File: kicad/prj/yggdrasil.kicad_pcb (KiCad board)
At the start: 2 copper layers, 186.8 x 135 mm, 44 parts, among them J2 4PIN, SW1 SW_PUSH, SW10 SW_PUSH, SW11 SW_PUSH, SW12 SW_PUSH, SW13 SW_PUSH, SW14 SW_PUSH, SW15 SW_PUSH, SW16 SW_PUSH, SW17 SW_PUSH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

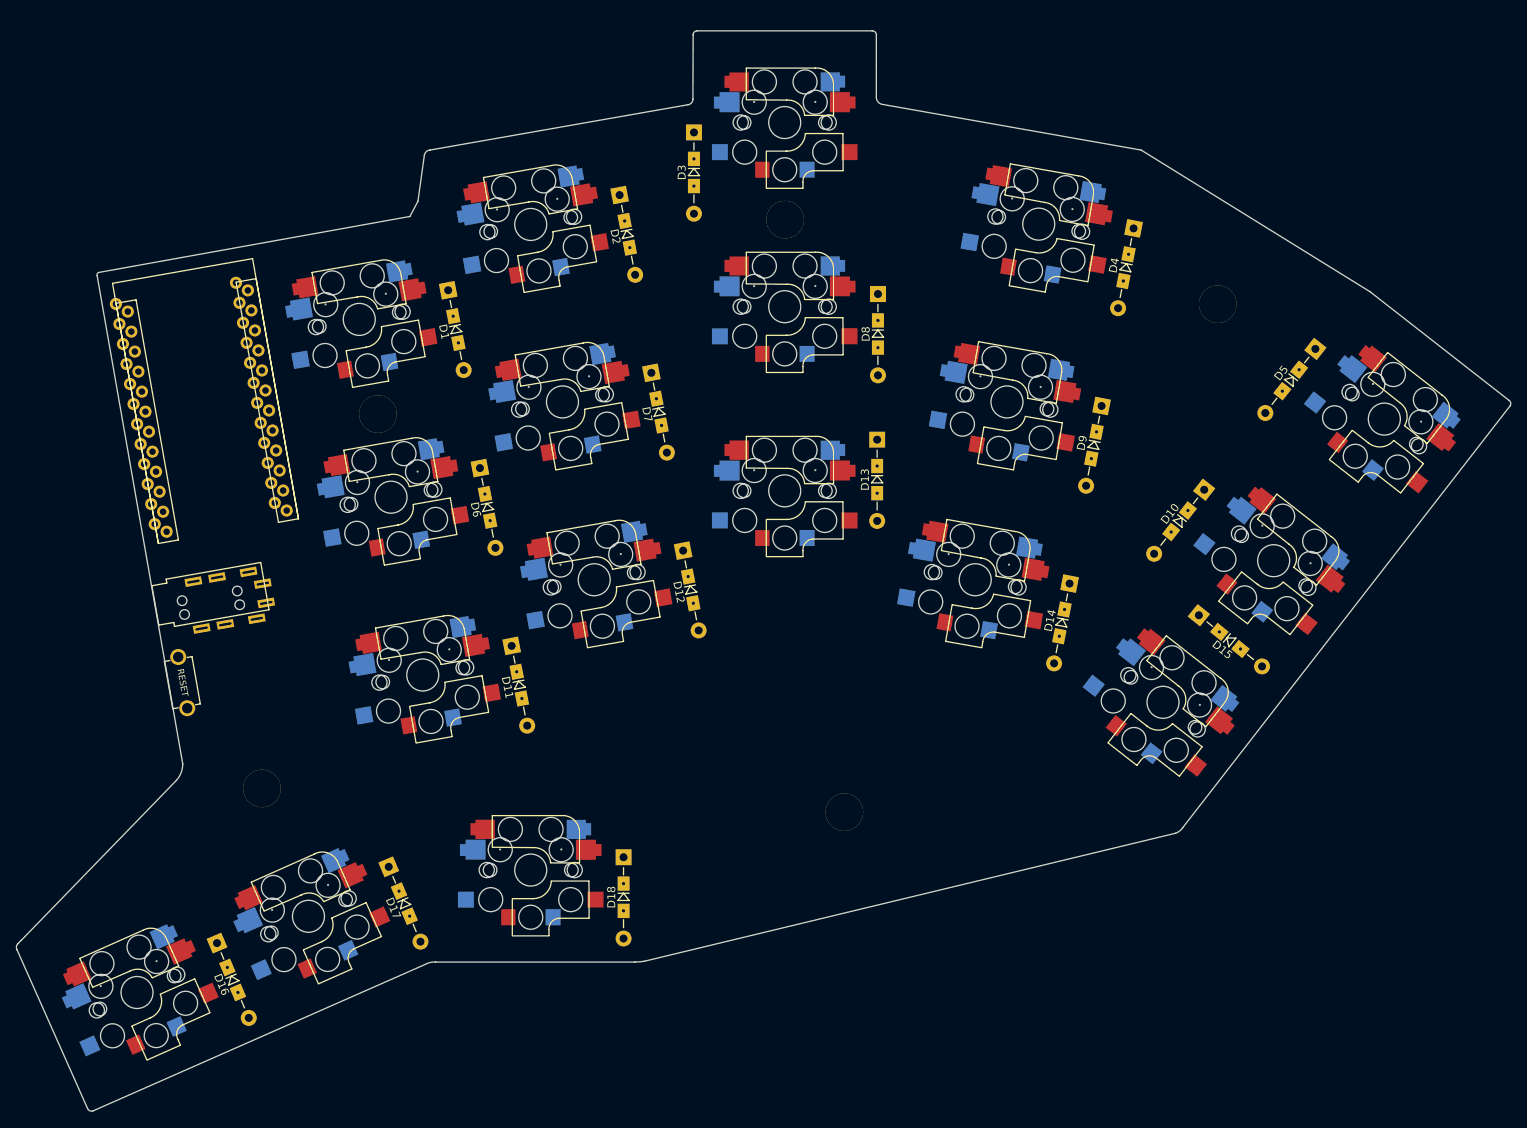
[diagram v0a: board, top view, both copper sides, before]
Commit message: Updated spacing Re-do edge cuts Some routing Diode placement Screwhole placement
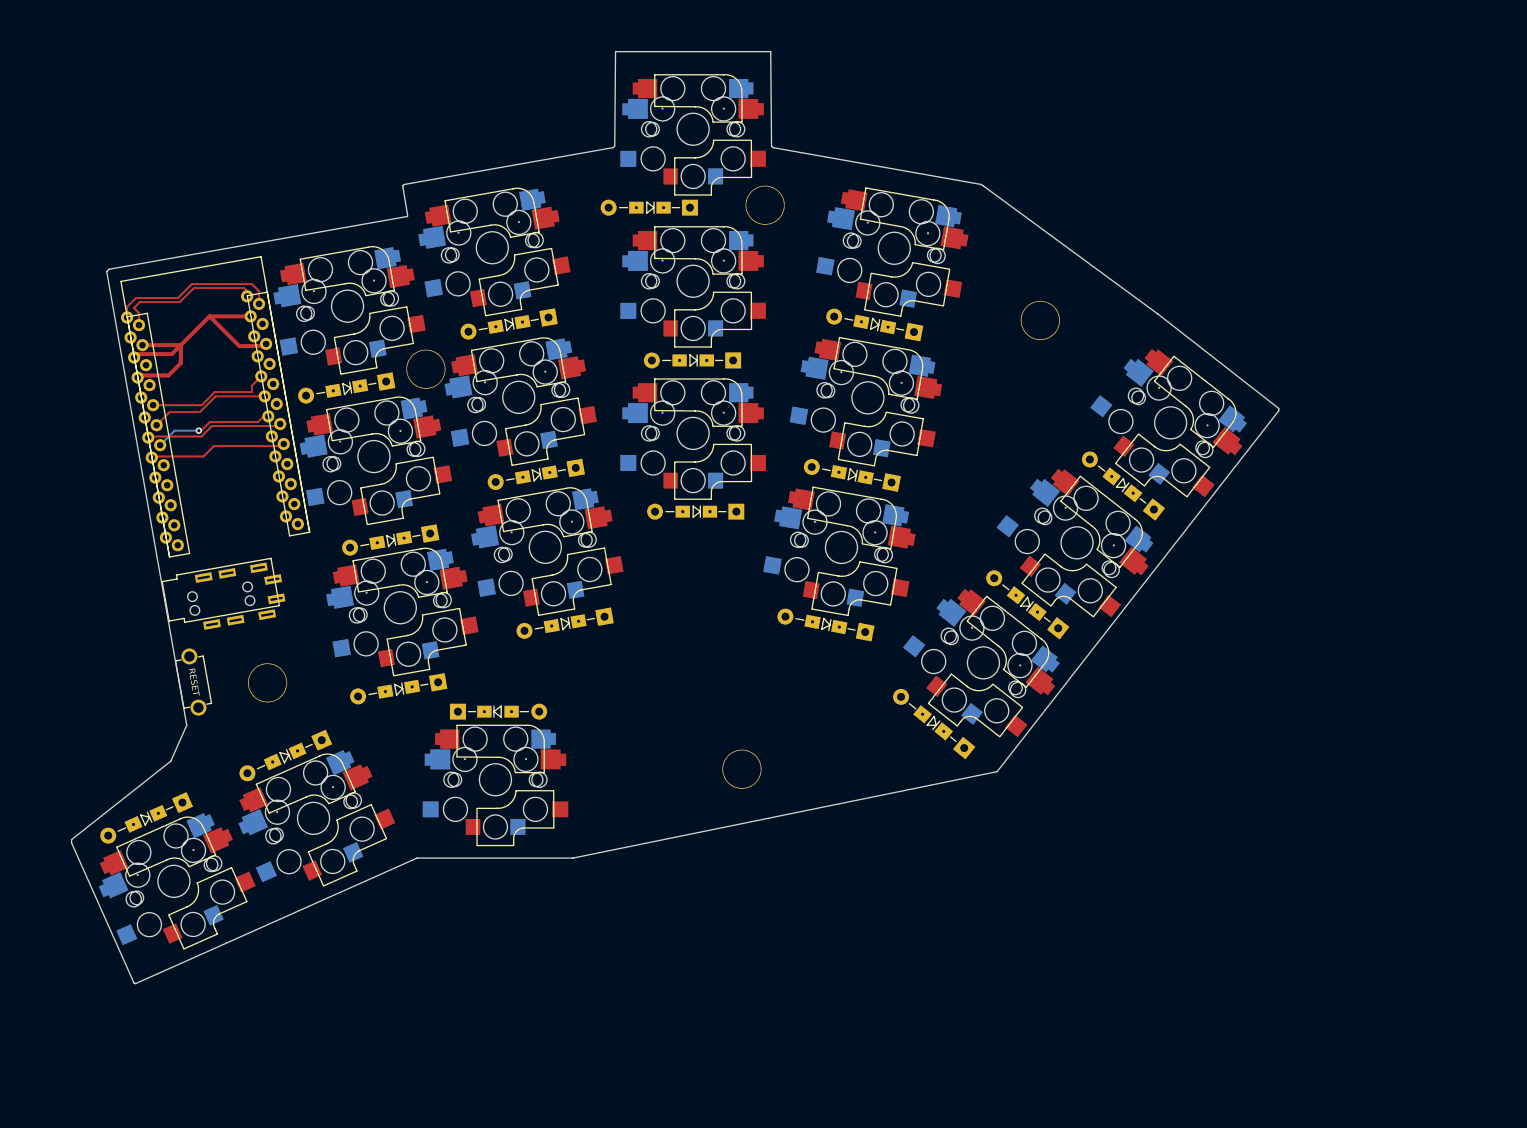
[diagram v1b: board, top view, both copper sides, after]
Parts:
- SW1, SW10, SW11, SW12, SW13, SW14, SW15, SW16, SW17, SW18, SW2, SW3, SW4, SW5, SW6, SW7, SW8, SW9: footprint Lily58-footprint:MX_Choc_Hotswap -> yggdrasil:Cherry_MX_Choc_Hotswap_MX_Spacing
- U1: footprint Lily58-footprint:ProMicro_rev2 -> yggdrasil:ProMicro_USB_C
- moved SW5 42.2 mm to (209.6, 85.0)
- moved SW10 40.0 mm to (197.9, 100.0)
- moved D15 38.5 mm to (195.4, 120.6), turned to 141 degrees
- moved SW15 38.0 mm to (186.2, 115.0)
- moved SW4 33.0 mm to (177.8, 70.2)
- moved D4 32.2 mm to (188.1, 70.8), turned to 169 degrees
- moved SW9 31.3 mm to (174.5, 88.9)
- moved D9 30.4 mm to (185.3, 89.6), turned to 169 degrees
- moved SW14 29.9 mm to (171.2, 107.6)
- moved D14 29.5 mm to (182.0, 108.3), turned to 169 degrees
- moved D18 28.0 mm to (141.0, 119.2), turned to 0 degrees
- moved SW3 25.4 mm to (154.4, 57.4)
- moved D5 24.8 mm to (219.1, 90.9), turned to 142 degrees
- moved SW8 23.8 mm to (154.4, 76.4)
- moved D17 23.7 mm to (114.4, 124.8), turned to -156 degrees
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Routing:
- net GND: track 0.00 -> 38.6 mm
- net unconnected-(U1-Pad1): track 0.00 -> 21.0 mm
- net unconnected-(U1-Pad24): track 0.00 -> 18.4 mm
- net unconnected-(U1-Pad8): track 0.00 -> 17.2 mm
- net unconnected-(U1-Pad7): track 0.00 -> 17.2 mm
- net unconnected-(U1-Pad20): track 0.00 -> 15.5 mm
- net unconnected-(U1-Pad19): track 0.00 -> 15.0 mm
- net unconnected-(U1-Pad18): track 0.00 -> 15.0 mm, vias 0 -> 1
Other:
- board size 186.8 x 135 mm -> 150.9 x 116.5 mm

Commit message: Change switch keycap spacing Add routing Add ground plane Add logo & text
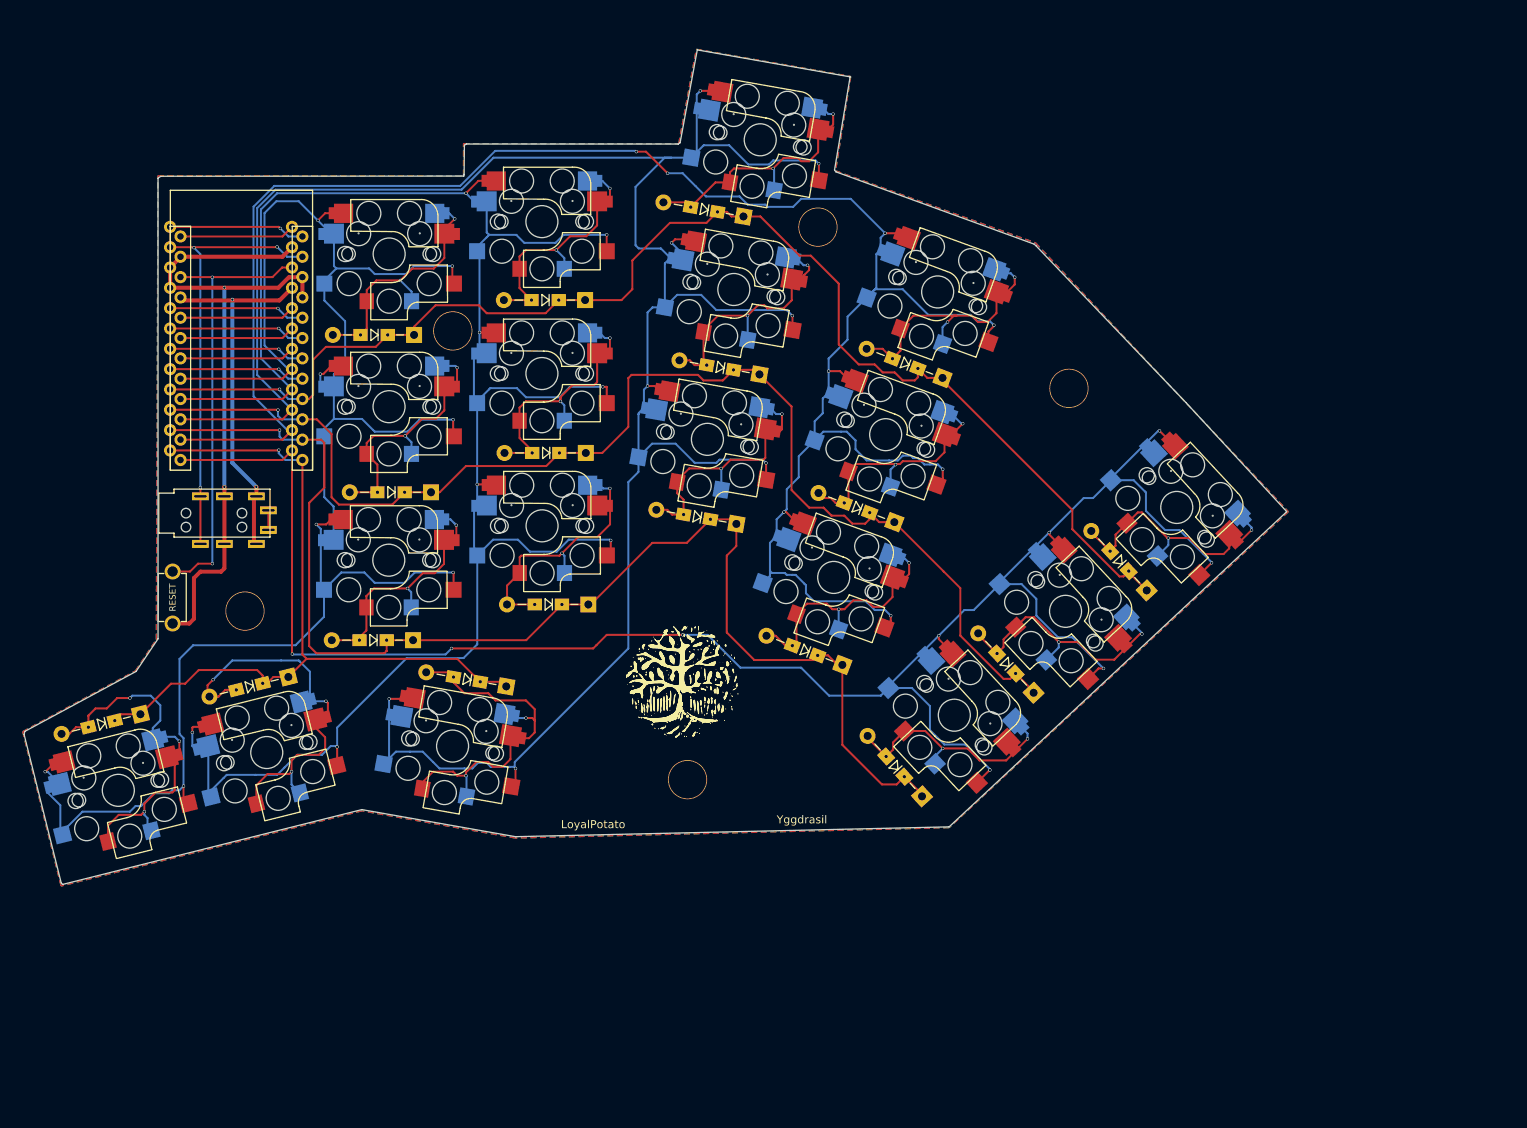
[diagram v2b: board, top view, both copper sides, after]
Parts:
- added G*** (x2): LOGO, yggdrasil:simple_logo, F.Cu at (164.1, 115.5)
- added G***: LOGO, yggdrasil:simple_logo, B.Cu at (164.1, 115.5)
- moved SW16 15.7 mm to (85.5, 142.4), turned to 14 degrees
- moved D16 13.1 mm to (91.5, 120.7), turned to -166 degrees
- moved SW17 12.5 mm to (104.1, 137.6), turned to 14 degrees
- moved U1 11.1 mm to (98.6, 89.0), turned to 0 degrees
- moved RSW1 10.9 mm to (100.3, 104.9), turned to 90 degrees
- moved J2 10.7 mm to (100.5, 94.4), turned to 90 degrees
- moved D17 9.80 mm to (109.9, 116.1), turned to -166 degrees
- moved D5 9.54 mm to (218.7, 100.4), turned to 133 degrees
- moved SW18 9.48 mm to (122.6, 132.4), turned to -10 degrees
- moved TH5 9.40 mm to (109.4, 106.6), turned to -10 degrees
- moved TH3 9.21 mm to (212.4, 78.8), turned to -10 degrees
- moved SW1 8.83 mm to (116.4, 73.0), turned to 0 degrees
- moved SW11 8.46 mm to (116.4, 111.3), turned to 0 degrees
- moved SW5 8.16 mm to (210.3, 93.1), turned to -47 degrees
- moved SW6 7.98 mm to (116.4, 92.1), turned to 0 degrees
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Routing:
- net col2: track 0.00 -> 309.3 mm, vias 0 -> 8
- net col3: track 0.00 -> 259.5 mm, vias 0 -> 8
- net col1: track 0.00 -> 255.4 mm, vias 0 -> 8
- net col0: track 0.00 -> 243.7 mm, vias 0 -> 8
- net col4: track 0.00 -> 241.3 mm, vias 0 -> 9
- net row0: track 0.00 -> 166.6 mm, vias 0 -> 1
- net row2: track 0.00 -> 162.6 mm, vias 0 -> 1
- net row1: track 0.00 -> 157.6 mm, vias 0 -> 1
- net row3: track 0.00 -> 97.9 mm, vias 0 -> 1
- net RESET: track 0.00 -> 55.6 mm, vias 0 -> 2
- net DATA: track 0.00 -> 54.4 mm, vias 0 -> 3
- net Net-(D17-Pad2): track 0.00 -> 52.1 mm, vias 0 -> 3
- net Net-(D16-Pad2): track 0.00 -> 47.5 mm, vias 0 -> 3
- net GND: track 38.6 -> 85.9 mm, vias 0 -> 2
- net VCC: track 0.00 -> 46.8 mm, vias 0 -> 2
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- added copper zone on B.Cu, net GND
- added copper zone on F.Cu, net GND
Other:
- board size 150.9 x 116.5 mm -> 157.8 x 104.3 mm
- board text added: "LoyalPotato"
- board text added: "Yggdrasil"

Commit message: Clean up/straighten routings
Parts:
- moved SW10 4.32 mm to (197.6, 102.0)
- moved D5 4.32 mm to (219.9, 96.2)
- moved J2 4.32 mm to (101.7, 90.2)
- moved D16 4.32 mm to (92.6, 116.6)
- moved SW18 4.32 mm to (123.8, 128.3)
- moved SW14 4.32 mm to (170.1, 104.8)
- moved D9 4.32 mm to (187.1, 89.6)
- moved D18 4.32 mm to (138.3, 111.0)
- moved D3 4.32 mm to (167.9, 52.3)
- moved G*** 4.32 mm to (165.3, 111.3) (x3)
- moved D4 4.32 mm to (193.1, 71.5)
- moved D12 4.32 mm to (148.5, 101.6)
- moved D10 4.32 mm to (205.7, 109.0)
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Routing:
- net col2: track 309.3 -> 297.2 mm
- net col3: track 259.5 -> 248.7 mm
- net col1: track 255.4 -> 261.9 mm
- net row0: track 166.6 -> 171.7 mm
- net Net-(D18-Pad2): track 46.0 -> 43.2 mm
- net Net-(D16-Pad2): track 47.5 -> 45.0 mm
- net Net-(D8-Pad2): track 34.0 -> 31.7 mm
- net col4: track 241.3 -> 239.6 mm
- net row3: track 97.9 -> 99.5 mm
- net Net-(D3-Pad2): track 36.1 -> 34.8 mm
- net Net-(D17-Pad2): track 52.1 -> 51.1 mm
- net row1: track 157.6 -> 156.6 mm
- net Net-(D9-Pad2): track 33.7 -> 32.7 mm
- net Net-(D4-Pad2): track 35.9 -> 35.0 mm
- net col0: track 243.7 -> 242.8 mm
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
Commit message: Prj files
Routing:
- net col3: track 248.7 -> 254.9 mm
